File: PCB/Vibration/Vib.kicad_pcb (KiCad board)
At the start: 2 copper layers, 60 x 110 mm, 15 parts, among them J1 Conn_01x02_Male, J2 Conn_01x02_Male, J3 Conn_01x02_Male, J4 Conn_01x02_Male, J5 Conn_01x03_Male, J6 Conn_01x03_Male, J7 Conn_01x03_Male, U1 ROB-14538, U2 ROB-14538, U3 ROB-14538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

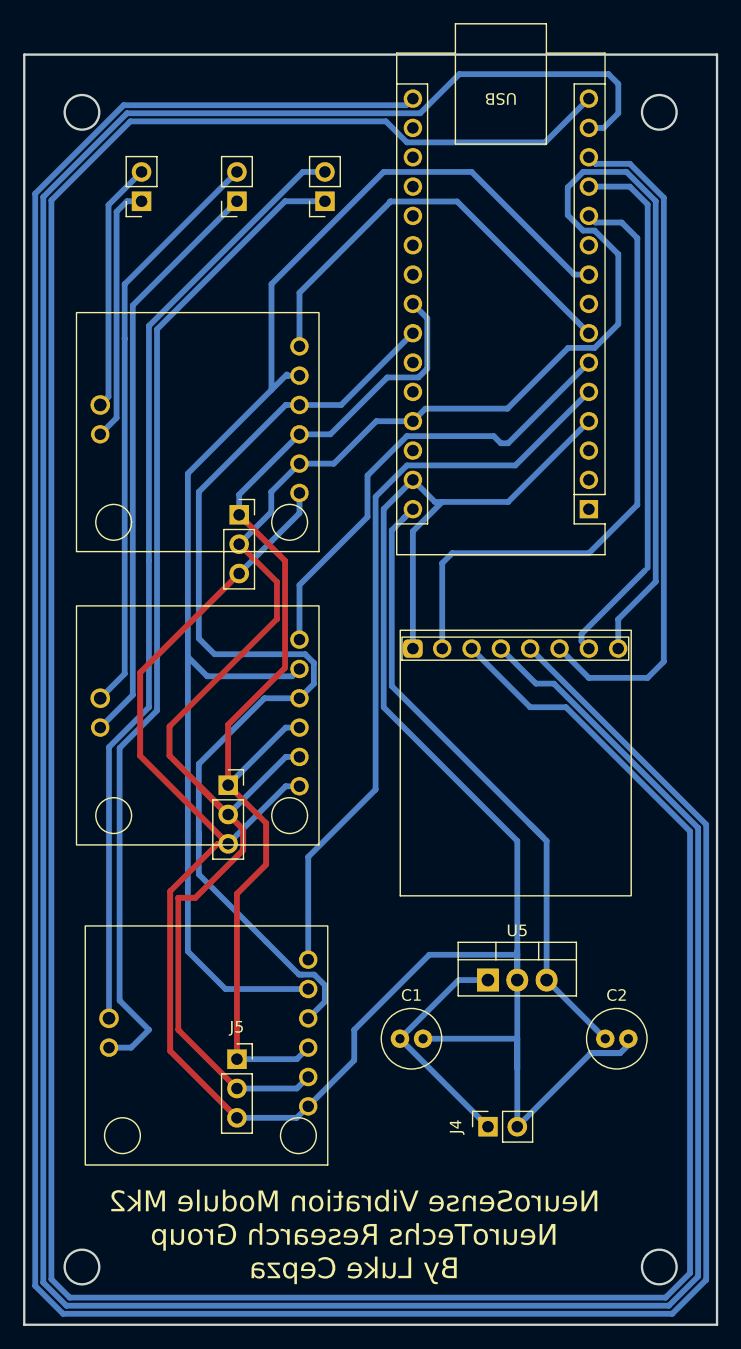
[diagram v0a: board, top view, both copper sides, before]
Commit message: Updated PCB files; added desing files for caress and vibration
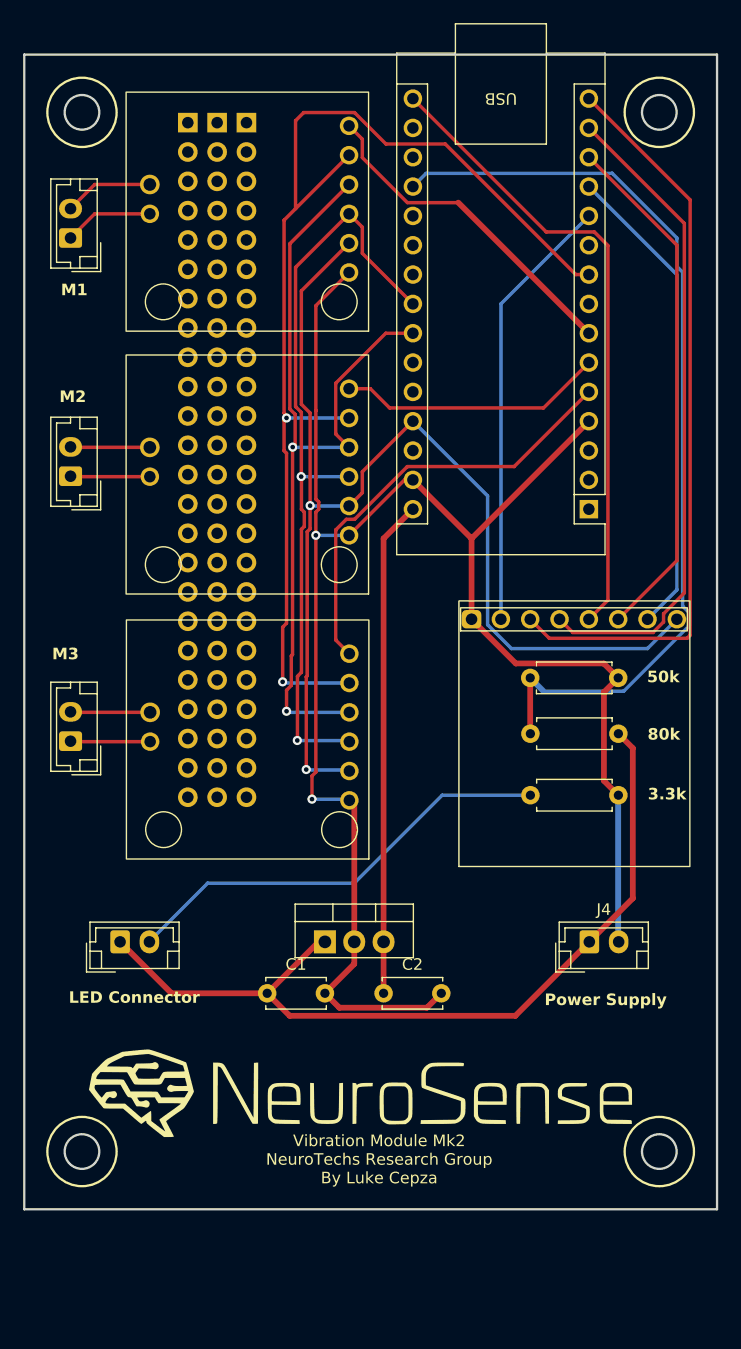
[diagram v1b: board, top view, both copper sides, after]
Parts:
- removed J5, J6, J7: Conn_01x03_Male, Connector_PinSocket_2.54mm:PinSocket_1x03_P2.54mm_Vertical
- added G***: LOGO, Logo:NeuroSenseLogo50mm, F.Cu at (69.5, 129.6)
- added LED Connector: Conn_01x02_Male, Connector_JST:JST_EH_B2B-EH-A_1x02_P2.50mm_Vertical, F.Cu at (48.3, 116.8)
- added R1: 80k, Resistor_THT:R_Axial_DIN0207_L6.3mm_D2.5mm_P7.62mm_Horizontal, F.Cu at (91.5, 98.8)
- added R2: 50K, Resistor_THT:R_Axial_DIN0207_L6.3mm_D2.5mm_P7.62mm_Horizontal, F.Cu at (83.8, 94.0)
- added R3: 3.3k, Resistor_THT:R_Axial_DIN0207_L6.3mm_D2.5mm_P7.62mm_Horizontal, F.Cu at (83.8, 104.1)
- added REF**: PinSocket_1x24_P2.54mm_Vertical, Connector_PinSocket_2.54mm:PinSocket_1x24_P2.54mm_Vertical, F.Cu at (59.2, 45.9)
- added REF**: PinSocket_1x24_P2.54mm_Vertical, Connector_PinSocket_2.54mm:PinSocket_1x24_P2.54mm_Vertical, F.Cu at (54.2, 45.9)
- added REF**: PinSocket_1x24_P2.54mm_Vertical, Connector_PinSocket_2.54mm:PinSocket_1x24_P2.54mm_Vertical, F.Cu at (56.7, 45.9)
- C1, C2: footprint Capacitor_THT:C_Radial_D5.0mm_H11.0mm_P2.00mm -> Capacitor_THT:C_Disc_D5.0mm_W2.5mm_P5.00mm
- J1, J2, J3, J4: footprint Connector_PinSocket_2.54mm:PinSocket_1x02_P2.54mm_Vertical -> Connector_JST:JST_EH_B2B-EH-A_1x02_P2.50mm_Vertical
- moved J1 51.7 mm to (44.0, 99.5), turned to 90 degrees
- moved J2 27.8 mm to (44.0, 76.5), turned to 90 degrees
- moved U1 26.7 mm to (69.8, 109.7)
- moved U2 22.1 mm to (69.8, 86.7)
- moved C2 19.6 mm to (71.1, 121.3)
- moved U3 19.6 mm to (69.8, 63.9)
- moved J4 18.3 mm to (88.9, 116.8), turned to 0 degrees
- moved U5 14.5 mm to (66.0, 116.8)
- moved C1 12.2 mm to (61.0, 121.3)
- moved J3 6.92 mm to (44.0, 55.9), turned to 90 degrees
- moved U4 5.68 mm to (78.6, 97.2)
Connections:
- net Net-(A1-Pad11) renamed /D8_IRQ
- net Net-(A1-Pad12) renamed /D9_CE
- net Net-(A1-Pad13) renamed /D10_CSN
- net Net-(A1-Pad14) renamed /D11_MOSI
- net Net-(A1-Pad15) renamed /D12_MISO
- net Net-(A1-Pad16) renamed /D13_SCK
- net Net-(A1-Pad24) renamed /A5_SCL
- net Net-(A1-Pad30) renamed /VIN_5v
- net Net-(A1-Pad9) renamed /D6_IN
- net Net-(C1-Pad1) renamed /v_BAT
- net Net-(J5-Pad1) renamed /A4_SDA
- net Net-(U1-Pad6) renamed /D2_EN2
- net Net-(U2-Pad6) renamed /D3_EN3
- net Net-(U3-Pad6) renamed /D4_EN4
- A1 pad 19: unconnected-(A1-Pad19) -> /A0_VBat
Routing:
- net /D11_MOSI: track 275.1 -> 56.8 mm
- net /D12_MISO: track 265.7 -> 64.8 mm
- net /D13_SCK: track 252.0 -> 55.2 mm
- net +5V: track 184.0 -> 102.8 mm, vias 0 -> 2
- net /A0_VBat: track 0.00 -> 81.2 mm
- net Net-(J1-Pin_1): track 86.3 -> 6.91 mm
- net Net-(J1-Pin_2): track 82.2 -> 6.89 mm
- net GND: track 231.6 -> 156.7 mm, vias 0 -> 2
- net /v_BAT: track 20.5 -> 72.9 mm
- net Net-(J2-Pin_2): track 50.5 -> 6.87 mm
- net Net-(J2-Pin_1): track 50.5 -> 6.88 mm
- net Net-(LED_Connector1-Pin_2): track 0.00 -> 38.3 mm
- net /A4_SDA: track 96.8 -> 66.9 mm, vias 0 -> 2
- net /D2_EN2: track 64.7 -> 38.1 mm
- net /D6_IN: track 121.4 -> 98.4 mm, vias 0 -> 2
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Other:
- board size 60 x 110 mm -> 60 x 100 mm
- board text added: "3.3k"
- board text added: "50k"
- board text added: "80k"
- board text added: "LED Connector"
- board text added: "M1"
- board text added: "M2"
- board text added: "M3"
- board text added: "Power Supply"
- board text added: "Vibration Module Mk2 NeuroTechs Research Group By Luke Cepza"
- board text removed: "NeuroSense Vibration Module Mk2 NeuroTechs Research Group By Luke Cepza"
